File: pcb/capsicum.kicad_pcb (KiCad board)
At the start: 2 copper layers, 68.6 x 88.9 mm, 70 parts, among them J2 Screw terminal, J3 USB-C 16+8 USB 2.0, Q1 NS2101P, Q2 BC817, SW1 SW_SPDT, SW3 SW_SPDT, U1 ESP32-C3-WROOM-02, U2 TQ33E-1, U3 AP2112K, U4 MCP73831

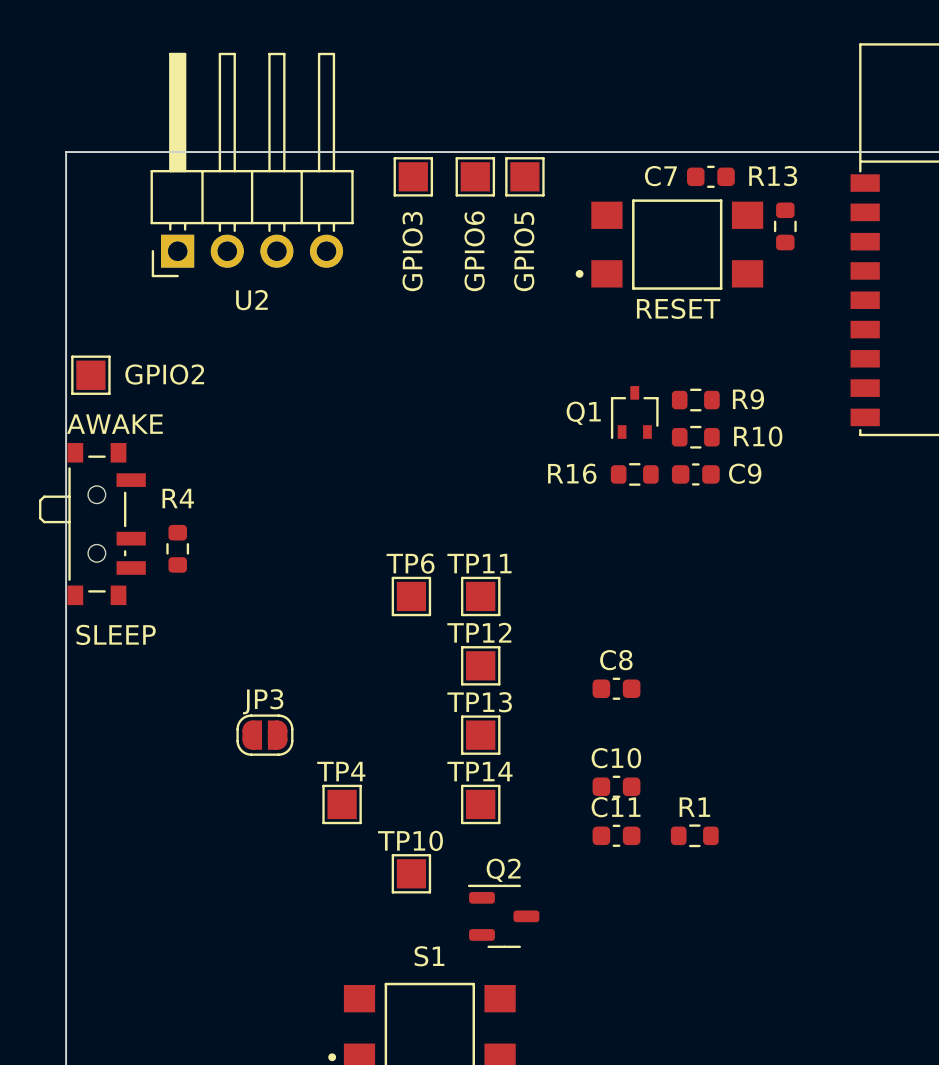
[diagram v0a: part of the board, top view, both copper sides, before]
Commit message: feat: group components from bell logical block in layout
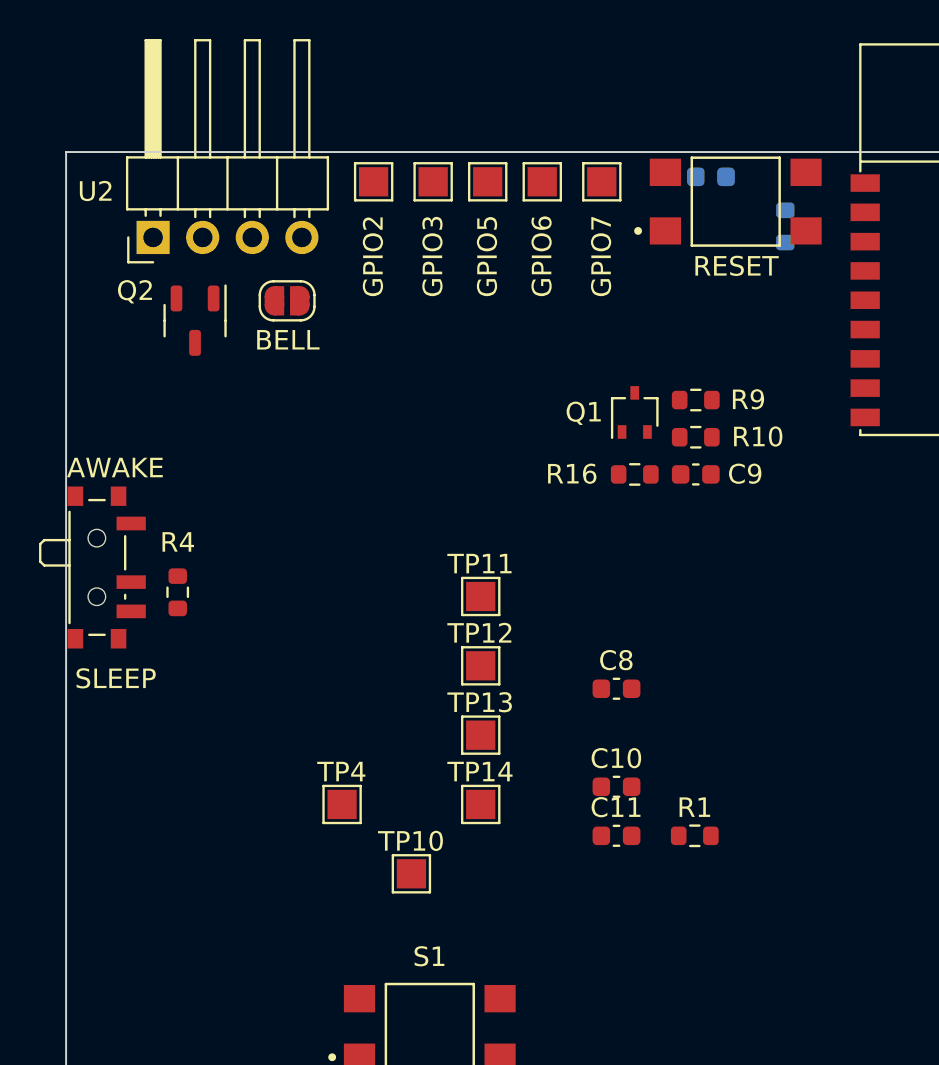
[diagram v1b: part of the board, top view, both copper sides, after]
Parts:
- C7, R13: moved to B.Cu
- moved Q2 34.4 mm to (110.7, 59.4), turned to -90 degrees
- moved TP6 23.4 mm to (131.6, 52.3)
- moved JP3 22.3 mm to (115.5, 58.4)
- moved TP5 17.5 mm to (119.9, 52.3), turned to -90 degrees
- moved S2 3.72 mm to (138.4, 53.3)
- moved TP8 3.44 mm to (128.5, 52.3)
- moved R4 2.22 mm to (109.9, 73.3)
- moved SW3 2.22 mm to (106.0, 72.1)
- moved TP9 1.92 mm to (125.7, 52.3)
- moved U2 1.44 mm to (108.6, 55.2)
- moved TP7 1.05 mm to (122.9, 52.3)
- turned C7 to 0 degrees

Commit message: feat: group components from bell connector logical block in layout
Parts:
- JP6, JP7, R11, R12, R3: moved to B.Cu
- moved R1 40.2 mm to (105.7, 111.8)
- moved TP4 33.1 mm to (127.0, 52.3)
- moved C8 27.1 mm to (114.3, 98.6), turned to -90 degrees
- moved S1 18.9 mm to (106.7, 105.6), turned to 90 degrees
- moved J2 9.94 mm to (108.5, 95.5)
- moved S2 3.81 mm to (142.2, 53.3)
- moved TP9 3.81 mm to (129.5, 52.3)
- moved U1 3.64 mm to (157.5, 58.3)
- moved TP8 3.56 mm to (132.1, 52.3)
- moved TP6 3.05 mm to (134.6, 52.3)
- moved TP5 2.03 mm to (121.9, 52.3)
- moved D1 1.65 mm to (168.7, 57.1)
- moved D4 1.65 mm to (168.7, 60.3)
- moved D5 1.65 mm to (168.7, 63.5)
- moved TP7 1.52 mm to (124.5, 52.3)

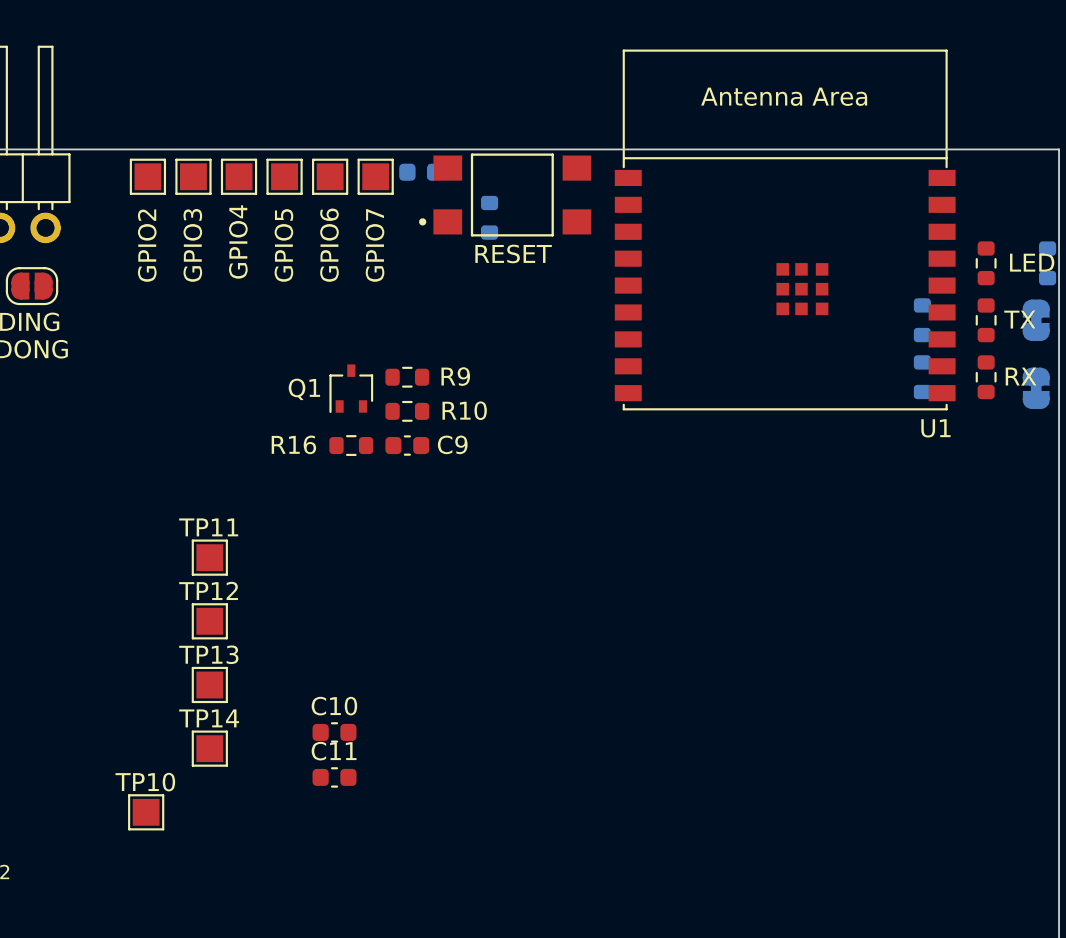
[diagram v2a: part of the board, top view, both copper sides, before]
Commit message: feat: group components from mcu logical block in layout
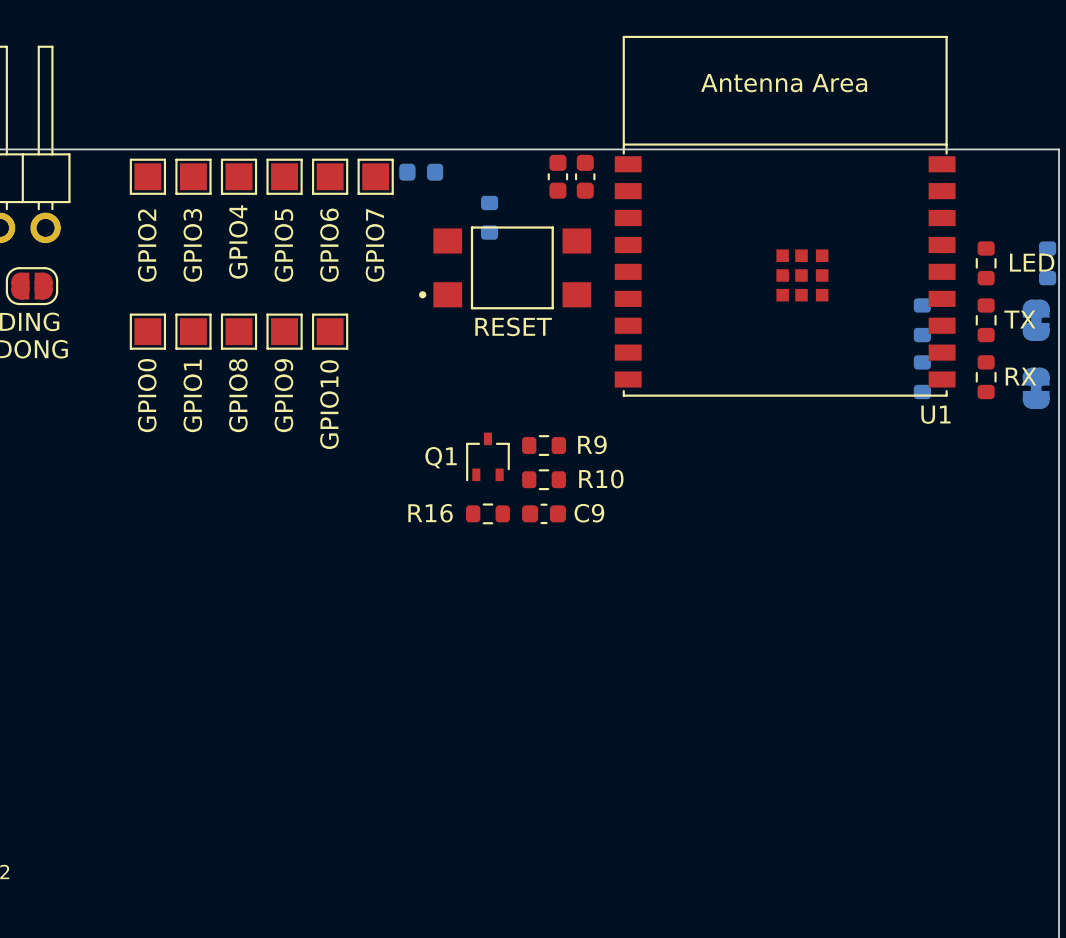
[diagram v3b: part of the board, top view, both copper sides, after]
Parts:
- moved C11 35.7 mm to (144.8, 52.3), turned to 90 degrees
- moved C10 34.0 mm to (146.3, 52.3), turned to 90 degrees
- moved TP10 27.3 mm to (127.0, 61.0)
- moved TP14 23.3 mm to (124.5, 61.0)
- moved TP13 20.0 mm to (121.9, 61.0)
- moved TP12 17.5 mm to (132.1, 61.0)
- moved TP11 13.3 mm to (129.5, 61.0)
- moved C9 8.52 mm to (144.0, 71.1)
- moved R10 8.52 mm to (144.0, 69.2)
- moved R16 8.52 mm to (140.9, 71.1)
- moved R9 8.52 mm to (144.0, 67.3)
- moved Q1 8.52 mm to (140.9, 67.9)
- moved S2 4.06 mm to (142.2, 57.4)
- moved U1 0.76 mm to (157.5, 57.5)

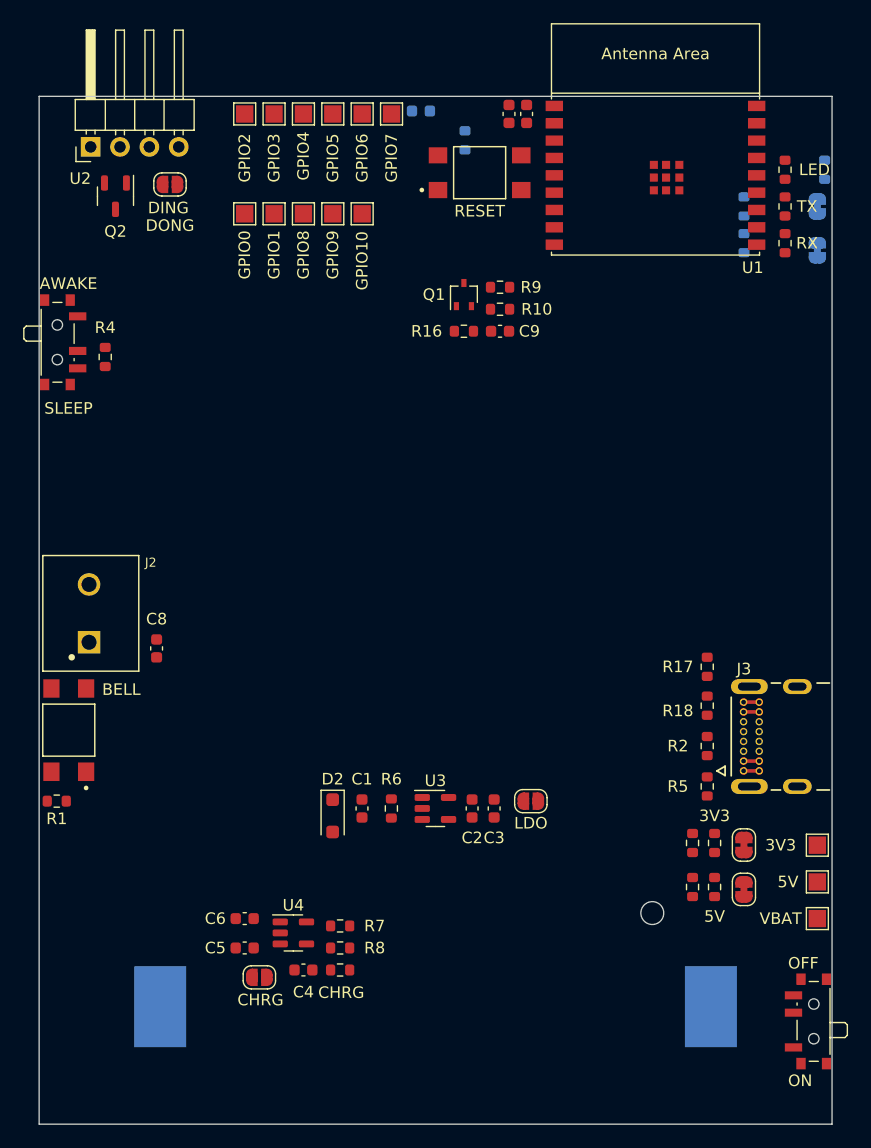
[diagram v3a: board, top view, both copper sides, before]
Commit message: feat: update layout, schematic and BOM with new test point for ground
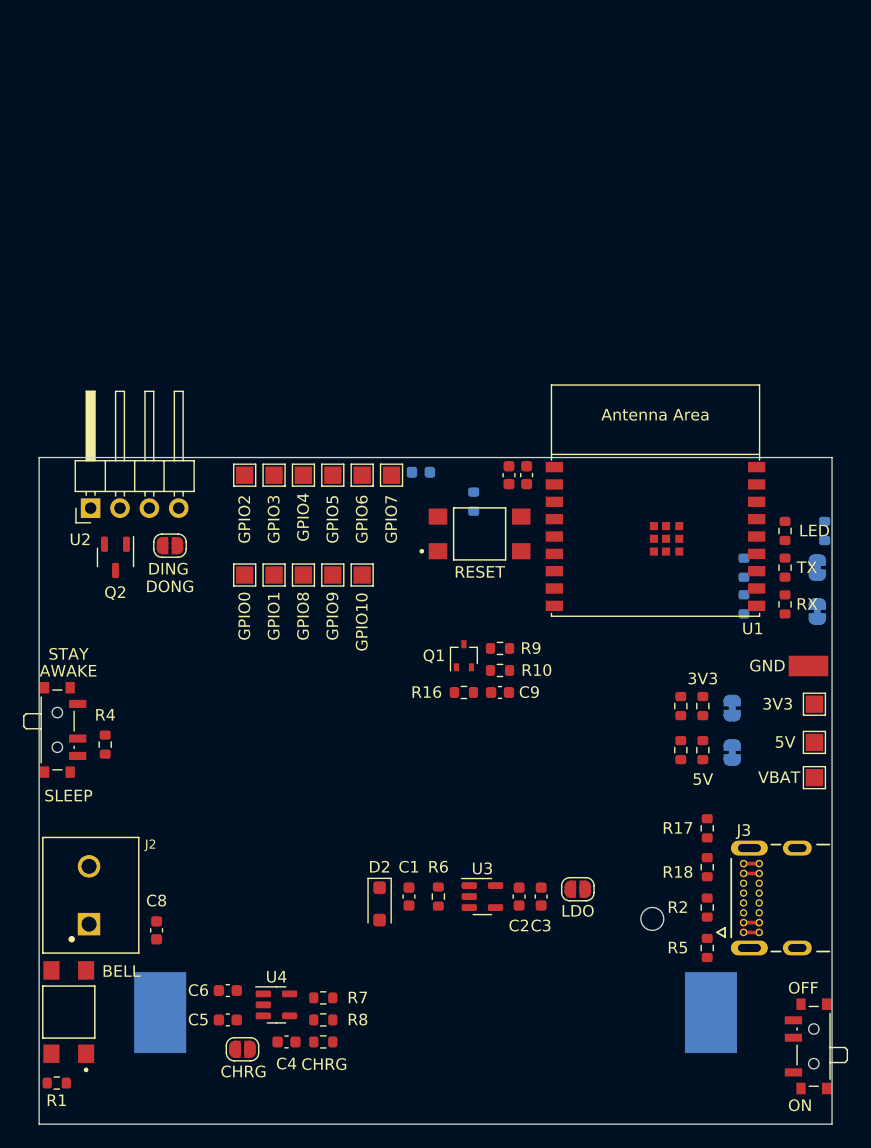
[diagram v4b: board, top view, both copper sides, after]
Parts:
- removed 5V, VBAT: TestPoint_Probe, TestPoint:TestPoint_Pad_1.5x1.5mm
- added TP1: TestPoint_Probe, TestPoint:TestPoint_Pad_1.5x1.5mm, F.Cu at (171.2, 106.7)
- added TP15: 5015, Keystone_TP:Keystone_test_point_5015, F.Cu at (170.7, 100.1)
- added TP2: TestPoint_Probe, TestPoint:TestPoint_Pad_1.5x1.5mm, F.Cu at (171.2, 109.7)
- JP4, JP5: moved to B.Cu
- moved SW3 33.5 mm to (106.0, 105.6)
- moved R4 33.5 mm to (109.9, 106.9)
- moved R13 31.3 mm to (141.7, 85.9)
- moved C10 31.2 mm to (146.3, 83.6)
- moved C11 31.2 mm to (144.8, 83.6)
- moved D5 31.2 mm to (168.7, 94.7)
- moved JP3 31.2 mm to (115.5, 89.7)
- moved Q1 31.2 mm to (140.9, 99.2)
- moved R12 31.2 mm to (165.1, 94.7)
- moved R9 31.2 mm to (144.0, 98.6)
- moved TP4 31.2 mm to (127.0, 83.6)
- moved TP5 31.2 mm to (121.9, 83.6)
- moved TP6 31.2 mm to (134.6, 83.6)
- moved TP7 31.2 mm to (124.5, 83.6)
- moved TP8 31.2 mm to (132.1, 83.6)
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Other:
- board size 68.6 x 88.9 mm -> 68.6 x 57.7 mm

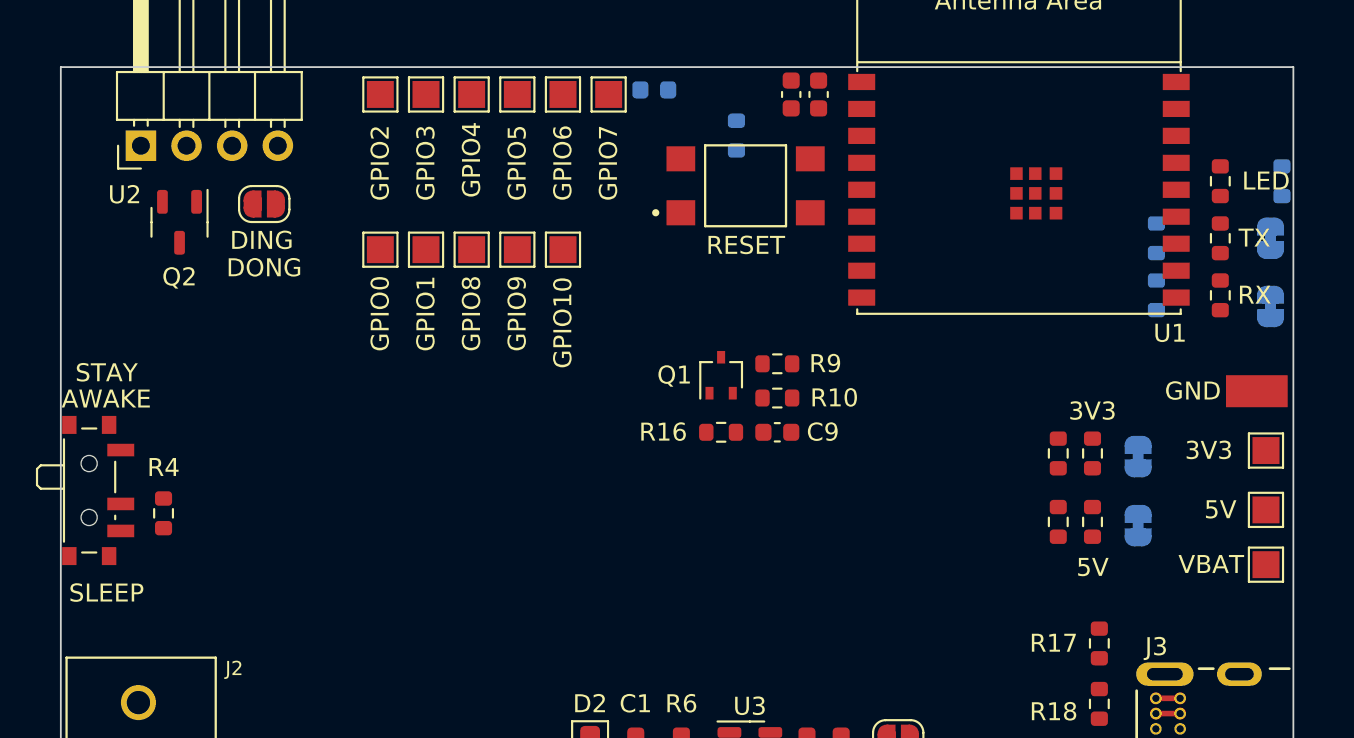
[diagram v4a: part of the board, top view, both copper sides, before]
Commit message: feat: add boot mode button in schematic, layout, BOM
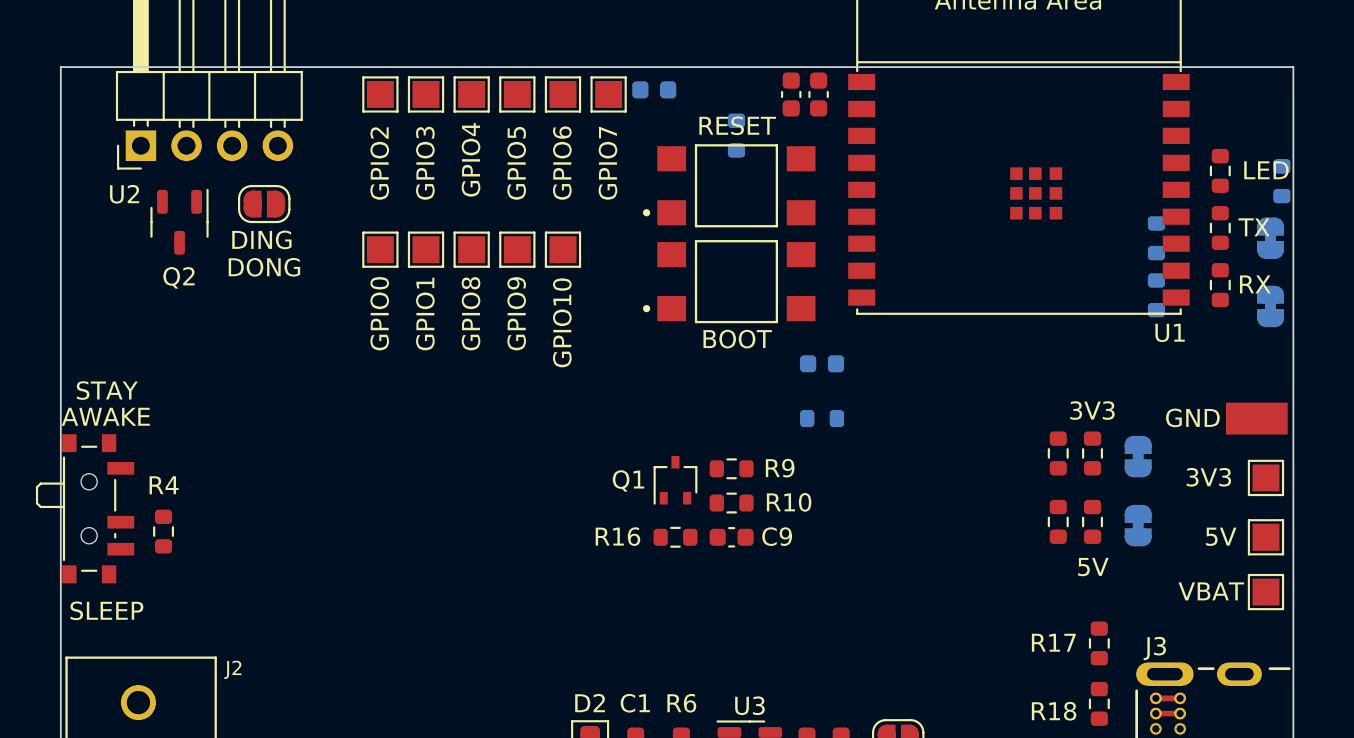
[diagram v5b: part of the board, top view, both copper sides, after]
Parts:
- added C12: 1uF, Capacitor_SMD:C_0603_1608Metric, B.Cu at (146.5, 98.6)
- added R19: 10k, Resistor_SMD:R_0603_1608Metric, B.Cu at (146.5, 101.6)
- added S3: Push button, Push button:SW_TL3305AF160QG, F.Cu at (141.7, 94.0)
- BT1: value 16320 battery -> 16320 / CR123A battery holder
- moved R10 6.37 mm to (141.5, 106.3)
- moved C9 6.37 mm to (141.5, 108.2)
- moved Q1 6.37 mm to (138.3, 105.0)
- moved R16 6.37 mm to (138.3, 108.2)
- moved R9 6.37 mm to (141.5, 104.4)
- moved TP15 1.52 mm to (170.7, 101.6)
- moved TP2 1.52 mm to (171.2, 111.3)
- moved TP3 1.52 mm to (171.2, 104.9)
- moved TP1 1.52 mm to (171.2, 108.2)
- moved R4 1.02 mm to (109.9, 107.9)
- moved SW3 1.02 mm to (106.0, 106.6)
- moved D1 0.57 mm to (168.7, 87.8)
- moved D4 0.57 mm to (168.7, 91.0)
- moved D5 0.57 mm to (168.7, 94.2)
- moved S2 0.51 mm to (141.7, 88.6)
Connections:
- net /B6 renamed /D+
- net /B7 renamed /D-
- net Net-(U1-GPIO9) renamed /BOOT
